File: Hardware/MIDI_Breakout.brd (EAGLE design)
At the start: 100 x 39.4 mm, 12 parts, among them U1 MIDIJACK, U2 MIDIJACK, U3 MIDIJACK, U4 6N138M

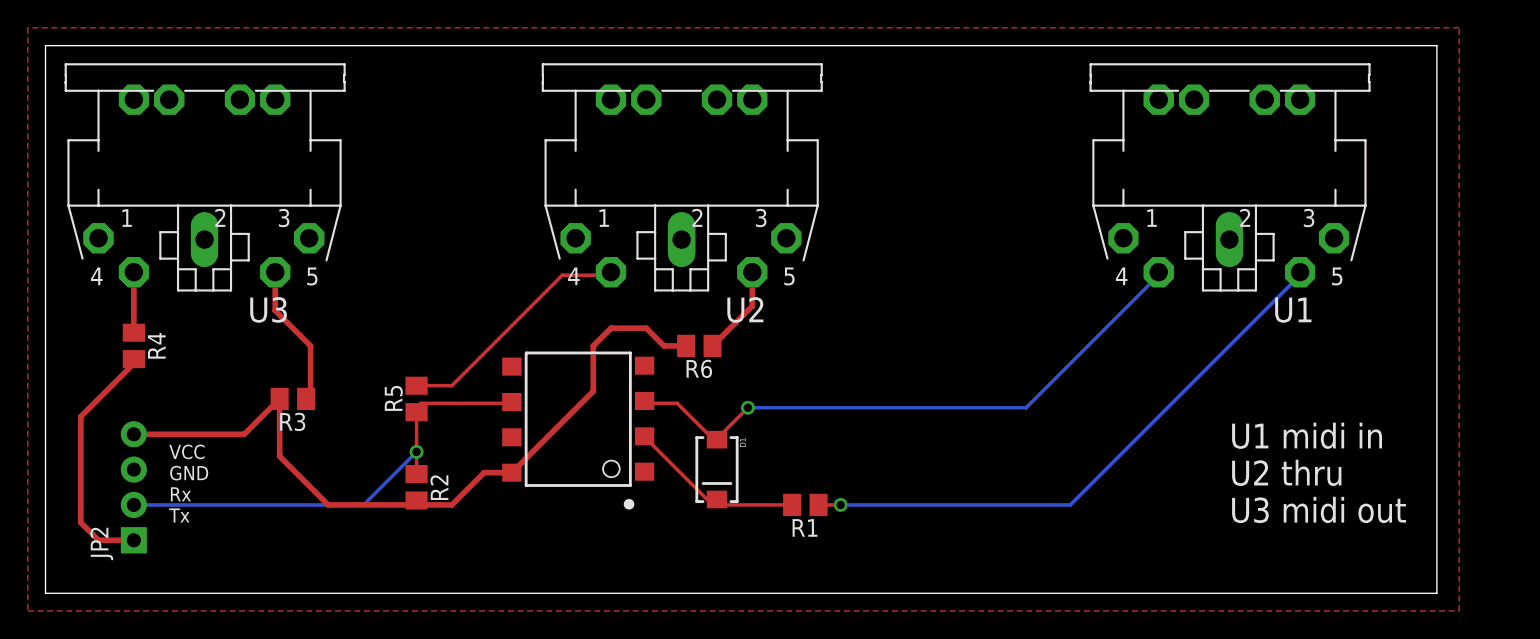
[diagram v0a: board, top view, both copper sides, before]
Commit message: mix thru hole and smd, layoutmostly
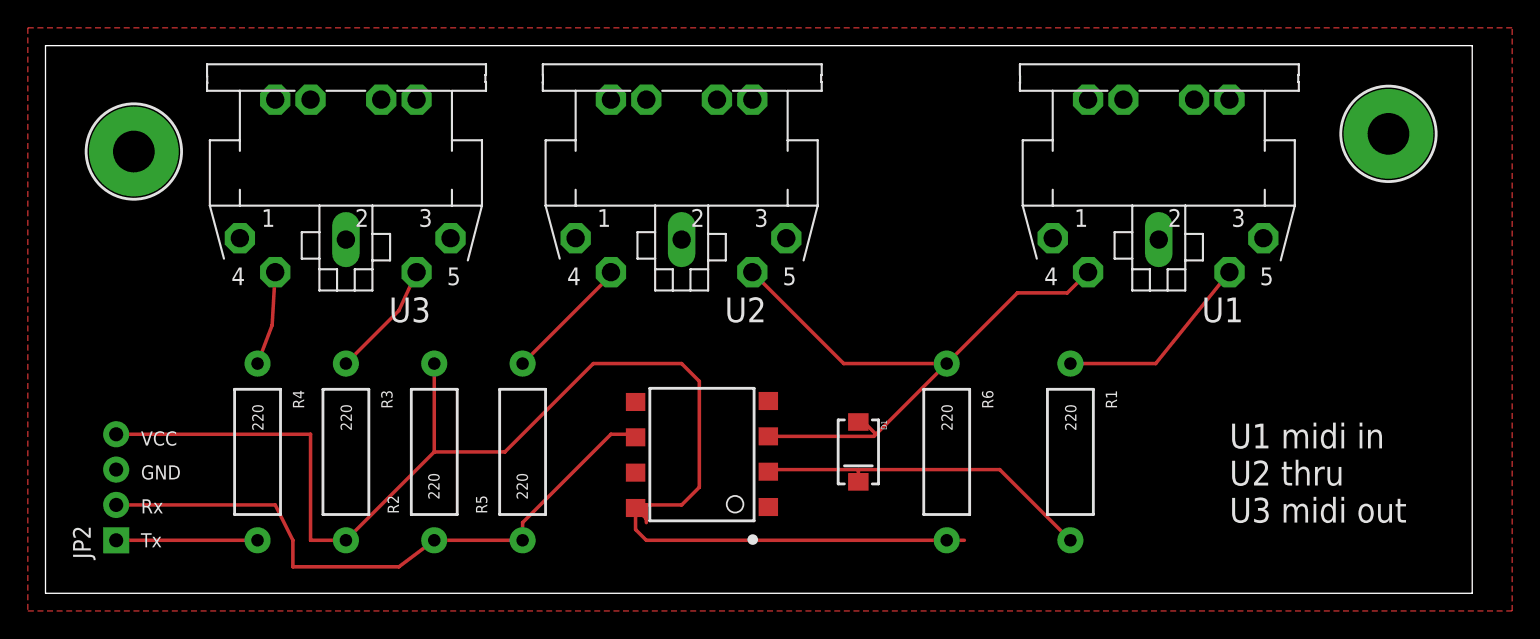
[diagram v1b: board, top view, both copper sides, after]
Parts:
- added U$1, U$2: MOUNTINGHOLE, microbuilder:MOUNTINGHOLE_3.0_PLATED
- R1, R2, R3, R4, R5, R6: device adafruit:M0805 -> SparkFun-Resistors:AXIAL-0.5
- moved R1 19.4 mm to (73.7, 10.2), turned to 270 degrees
- moved R6 19.3 mm to (64.8, 10.2), turned to 270 degrees
- moved R4 11.7 mm to (15.2, 10.2)
- moved D1 10.2 mm to (58.4, 10.2)
- moved U3 10.2 mm to (21.6, 38.1)
- moved U4 9.25 mm to (47.0, 10.2)
- moved R5 8.52 mm to (34.3, 10.2)
- moved R3 5.39 mm to (21.6, 10.2), turned to 270 degrees
- moved U1 5.08 mm to (80.0, 38.1)
- moved R2 2.84 mm to (27.9, 10.2), turned to 90 degrees
- moved JP2 1.27 mm to (5.08, 3.81)
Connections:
- net 1235: now also R3.P$1; no longer R3.1
- net 56: now also R1.P$2; no longer R1.2
- net N$1: now also R6.P$1; no longer R6.1
- net N$2: now also R5.P$2; no longer R5.2
- net N$3: now also R1.P$1; no longer R1.1
- net N$8: now also R4.P$1; no longer R4.1
- net RX: now also R2.P$1, R5.P$1; no longer R2.1, R5.1
- net TX: now also R4.P$2; no longer R4.2
- net VCC: now also R2.P$2, R3.P$2, R6.P$2; no longer R2.2, R3.2, R6.2
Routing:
- net VCC: track 54.3 -> 101.5 mm
- net N$3: track 41.7 -> 14.6 mm, vias 1 -> 0
- net PIN5: track 43.6 -> 29.5 mm, vias 1 -> 0
- net 56: track 12.7 -> 24.8 mm
- net RX: track 33.7 -> 45.4 mm, vias 1 -> 0
- net N$1: track 6.48 -> 16.7 mm
- net N$2: track 17.5 -> 9.20 mm
- net TX: track 17.7 -> 10.2 mm
- net N$8: track 4.35 -> 6.77 mm
- net 1235: track 10.3 -> 8.43 mm
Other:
- board size 100 x 39.4 mm -> 102.5 x 39.4 mm
